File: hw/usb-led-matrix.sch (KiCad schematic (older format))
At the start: 103 parts, among them J1 USB_C_Receptacle_USB2.0, J2 Conn_ST_STDC14, U1 AP2210K-3.3, U2 STM32G473CET6, U3 74LVT245, U4 USBLC6-2P6, Y1 Crystal_GND24

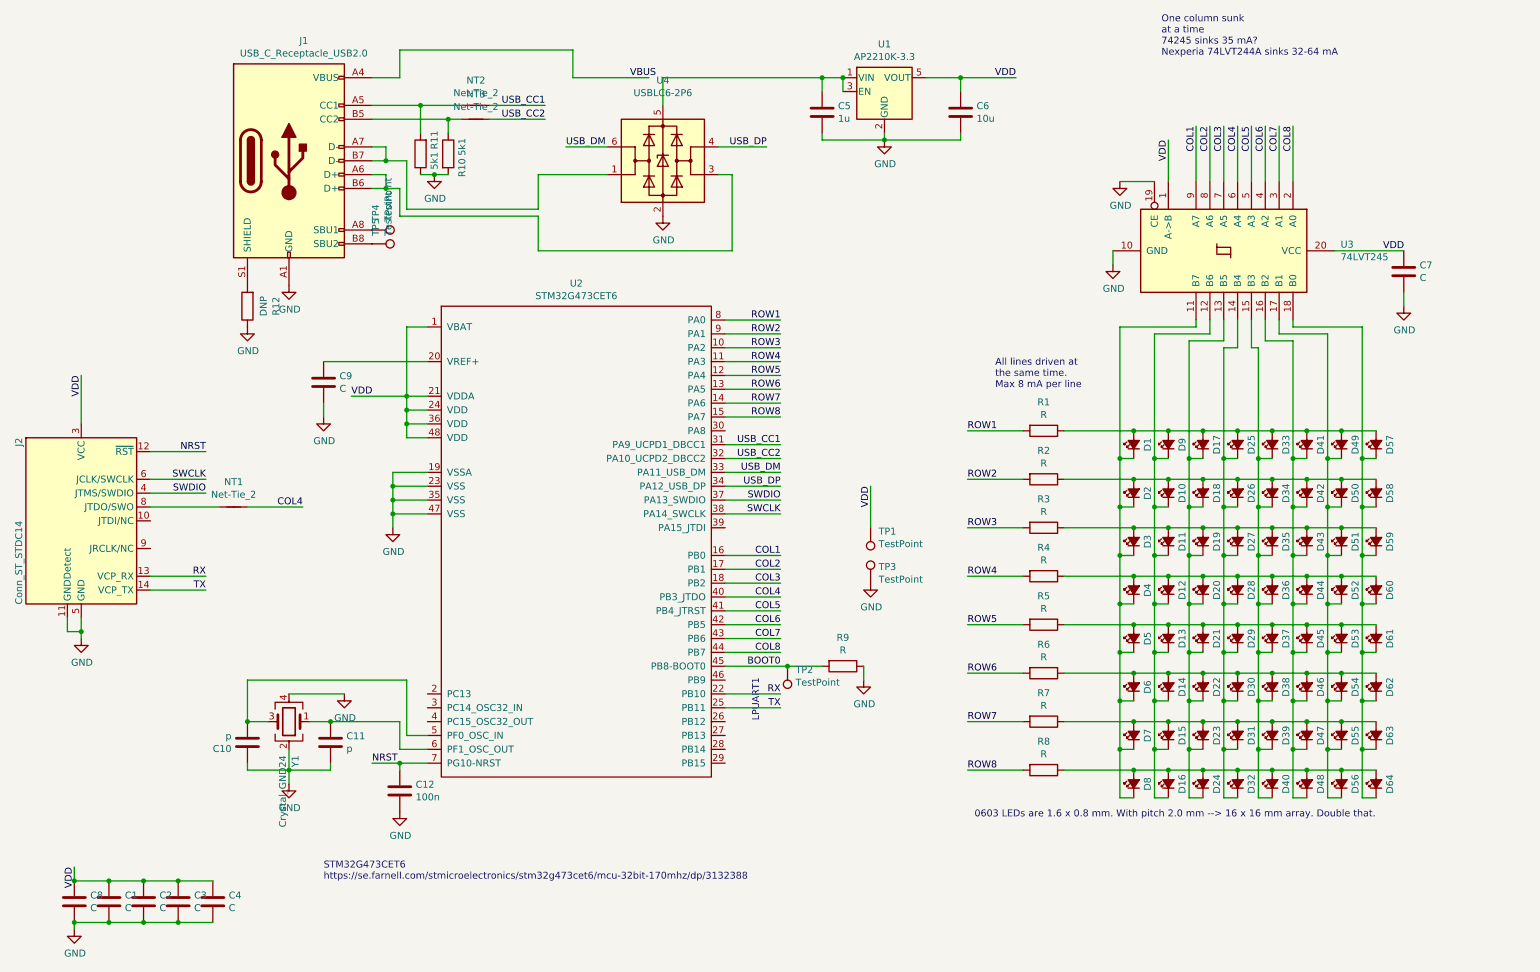
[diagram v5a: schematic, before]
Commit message: Four-layer board, update routing and some components
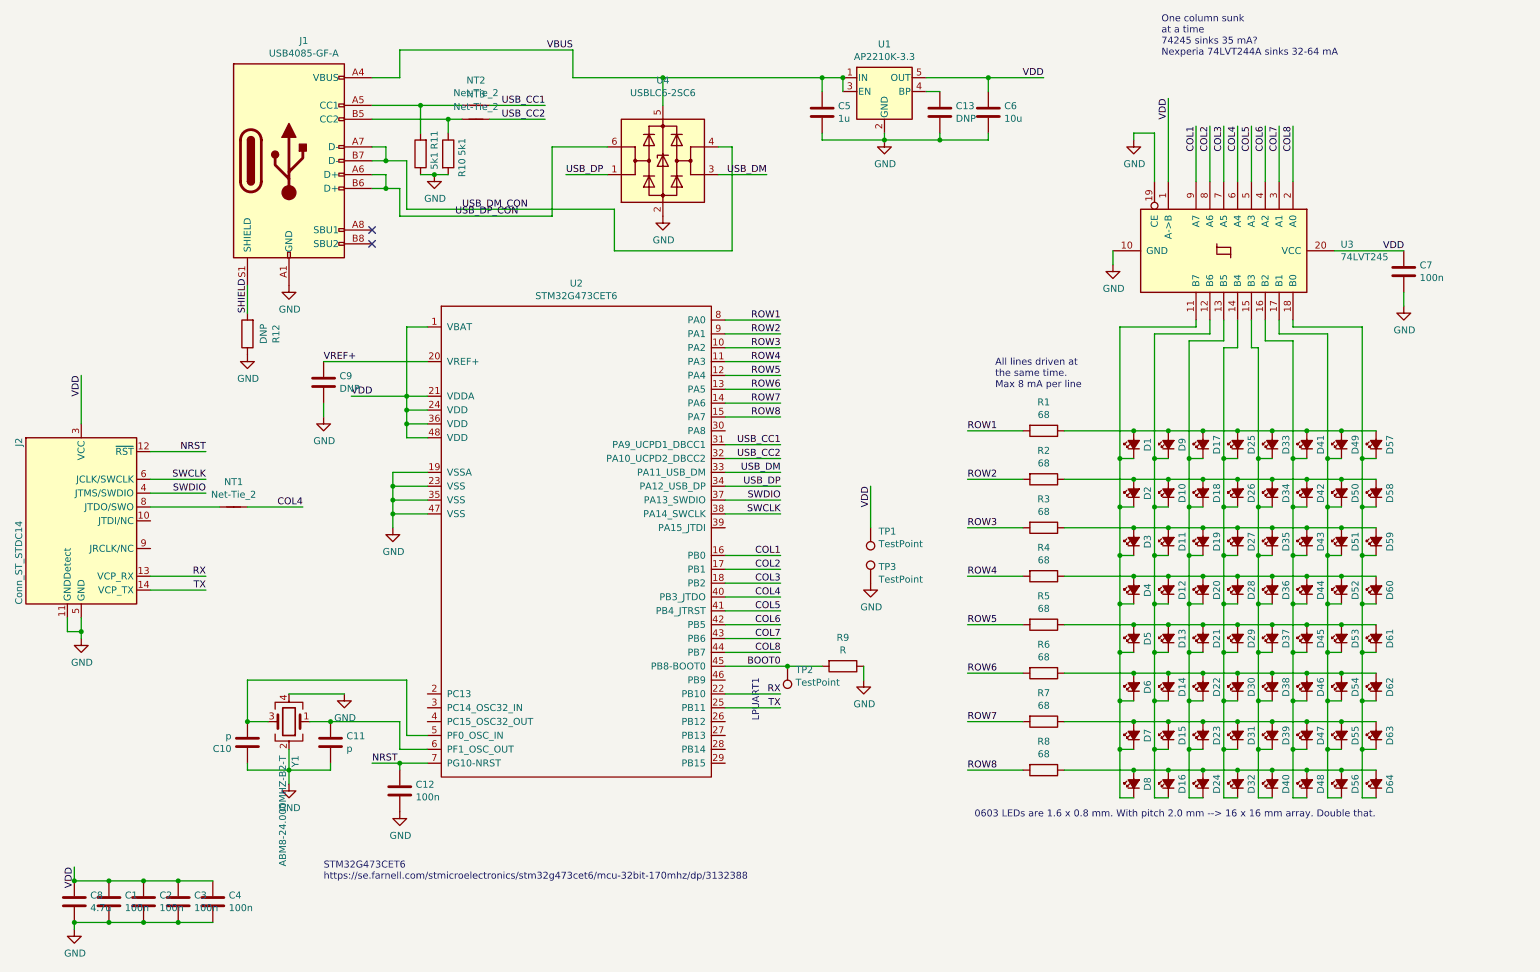
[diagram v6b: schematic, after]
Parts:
- removed TP4, TP5: TestPoint, TestPoint:TestPoint_Pad_1.0x1.0mm, symbol Connector:TestPoint
- removed U1: AP2210K-3.3, Package_TO_SOT_SMD:SOT-23-5, symbol Regulator_Linear:AP2204K-3.3
- removed U4: USBLC6-2P6, Package_TO_SOT_SMD:SOT-666, symbol Power_Protection:USBLC6-2P6
- added C13: DNP, Capacitor_SMD:C_0402_1005Metric_Pad0.74x0.62mm_HandSolder, symbol Device:C
- added U1: AP2210K-3.3, Package_TO_SOT_SMD:SOT-23-5, symbol Regulator_Linear:AP131-33
- added U4: USBLC6-2SC6, Package_TO_SOT_SMD:SOT-23-6, symbol Power_Protection:USBLC6-2SC6
- C1, C2, C3, C4, C7: value C -> 100n
- C8: value C -> 4.7u
- C9: value C -> DNP
- J1: value USB_C_Receptacle_USB2.0 -> USB4085-GF-A
- NT1, NT2, NT3: footprint NetTie:NetTie-2_SMD_Pad0.5mm -> Resistor_SMD:R_0201_0603Metric
- R1, R2, R3, R4, R5, R6, R7, R8: value R -> 68
- Y1: value Crystal_GND24 -> ABM8-24.000MHZ-B2-T
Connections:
- net GND: now also C13.2, U1.2 (GND), U4.2 (GND)
- net USB_DM: now also U4.3 (I/O2)
- net USB_DP: now also U4.1 (I/O1)
- net VBUS: now also C5.1, J1.A4 (VBUS), J1.A9 (VBUS), J1.B4 (VBUS), J1.B9 (VBUS), U1.1 (IN), U1.3 (EN), U4.5 (VBUS)
- net VDD: now also U1.5 (OUT)
- net USB_DP_CON: now reaches J1.A6 (D+), J1.B6 (D+)
- net USB_DP_CON: now also U4.6 (I/O1)
- net USB_DM_CON: now reaches J1.A7 (D-), J1.B7 (D-)
- net USB_DM_CON: now also U4.4 (I/O2)
- net SHIELD: now reaches J1.S1 (SHIELD), R12.2
- net VREF+: now reaches C9.1, U2.20 (VREF+)
- new net: C13.1, U1.4 (BP)
- no-connect marks 0 -> 2
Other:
- moved on the sheet: C6, R12

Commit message: Rearrange pins
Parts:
- removed NT1: Net-Tie_2, Resistor_SMD:R_0201_0603Metric, symbol Device:Net-Tie_2
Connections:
- net BOOT0 is gone; now on net ROW1: R9.2, TP2.1, U2.45 (PB8-BOOT0)
- net ROW1: no longer U2.8 (PA0)
- net ROW2: now also U2.46 (PB9); no longer U2.9 (PA1)
- net ROW3: now also U2.22 (PB10); no longer U2.10 (PA2)
- net ROW4: now also U2.25 (PB11); no longer U2.11 (PA3)
- net ROW5: now also U2.26 (PB12); no longer U2.12 (PA4)
- net ROW6: now also U2.27 (PB13); no longer U2.13 (PA5)
- net ROW7: now also U2.28 (PB14); no longer U2.14 (PA6)
- net ROW8: now also U2.29 (PB15); no longer U2.15 (PA7)
- net RX: now also U2.11 (PA3); no longer U2.22 (PB10)
- net TX: now also U2.10 (PA2); no longer U2.25 (PB11)
- no-connect marks 2 -> 5
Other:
- moved on the sheet: R9, TP2
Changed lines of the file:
@@
 USB_DP
 Wire Wire Line
-	5900 2850 6300 2850
-Wire Wire Line
-	5900 2950 6300 2950
-Wire Wire Line
-	5900 3050 6300 3050
-Wire Wire Line
-	5900 3150 6300 3150
-Wire Wire Line
-	5900 3250 6300 3250
-Wire Wire Line
-	5900 3350 6300 3350
-Wire Wire Line
-	5900 3450 6300 3450
-Wire Wire Line
-	5900 3550 6300 3550
-Text Label 6300 2850 2    50   ~ 0
+	5900 5450 6300 5450
+Wire Wire Line
+	5900 5550 6300 5550
+Wire Wire Line
+	5900 5650 6300 5650
+Wire Wire Line
+	5900 5750 6300 5750
+Wire Wire Line
+	5900 5850 6300 5850
+Wire Wire Line
+	5900 5950 6300 5950
+Wire Wire Line
+	5900 6050 6300 6050
+Text Label 6300 5350 2    50   ~ 0
 ROW1
-Text Label 6300 2950 2    50   ~ 0
+Text Label 6300 5450 2    50   ~ 0
 ROW2
-Text Label 6300 3050 2    50   ~ 0
+Text Label 6300 5550 2    50   ~ 0
 ROW3
-Text Label 6300 3150 2    50   ~ 0
+Text Label 6300 5650 2    50   ~ 0
 ROW4
-Text Label 6300 3250 2    50   ~ 0
+Text Label 6300 5750 2    50   ~ 0
 ROW5
-Text Label 6300 3350 2    50   ~ 0
+Text Label 6300 5850 2    50   ~ 0
 ROW6
-Text Label 6300 3450 2    50   ~ 0
+Text Label 6300 5950 2    50   ~ 0
 ROW7
-Text Label 6300 3550 2    50   ~ 0
+Text Label 6300 6050 2    50   ~ 0
 ROW8
 Wire Wire Line
@@
 L Device:R R9
 U 1 1 6036EDA7
-P 6750 5350
-F 0 "R9" V 6543 5350 50  0000 C CNN
-F 1 "R" V 6634 5350 50  0000 C CNN
-F 2 "Resistor_SMD:R_0402_1005Metric_Pad0.72x0.64mm_HandSolder" V 6680 5350 50  0001 C CNN
-F 3 "~" H 6750 5350 50  0001 C CNN
-	1    6750 5350
+P 7100 5350
+F 0 "R9" V 6893 5350 50  0000 C CNN
+F 1 "R" V 6984 5350 50  0000 C CNN
+F 2 "Resistor_SMD:R_0402_1005Metric_Pad0.72x0.64mm_HandSolder" V 7030 5350 50  0001 C CNN
+F 3 "~" H 7100 5350 50  0001 C CNN
+	1    7100 5350
 	0    1    1    0
 $EndComp
 Wire Wire Line
-	5900 5350 6350 5350
-Text Label 6300 5350 2    50   ~ 0
-BOOT0
-Wire Wire Line
-	5900 5650 6300 5650
-Wire Wire Line
-	5900 5550 6300 5550
-Text Label 6300 5650 2    50   ~ 0
+	5900 3050 6300 3050
+Wire Wire Line
+	5900 3150 6300 3150
+Text Label 6300 3050 2    50   ~ 0
 TX
 $Comp
@@
 Text Label 4800 900  2    50   ~ 0
 VBUS
-Text Label 6300 5550 2    50   ~ 0
+Text Label 6300 3150 2    50   ~ 0
 RX
 $Comp
@@
 L power:GND #PWR0109
 U 1 1 6068EE74
-P 6900 5450
-F 0 "#PWR0109" H 6900 5200 50  0001 C CNN
-F 1 "GND" H 6905 5277 50  0000 C CNN
-F 2 "" H 6900 5450 50  0001 C CNN
-F 3 "" H 6900 5450 50  0001 C CNN
-	1    6900 5450
-	1    0    0    -1
-$EndComp
-Wire Wire Line
-	6900 5350 6900 5450
+P 7250 5450
+F 0 "#PWR0109" H 7250 5200 50  0001 C CNN
+F 1 "GND" H 7255 5277 50  0000 C CNN
+F 2 "" H 7250 5450 50  0001 C CNN
+F 3 "" H 7250 5450 50  0001 C CNN
+	1    7250 5450
+	1    0    0    -1
+$EndComp
+Wire Wire Line
+	7250 5350 7250 5450
 $Comp
 L Device:C C9
@@
 L Connector:TestPoint TP2
 U 1 1 6086B887
-P 6350 5350
-F 0 "TP2" H 6292 5376 50  0000 R CNN
-F 1 "TestPoint" H 6292 5467 50  0000 R CNN
-F 2 "TestPoint:TestPoint_THTPad_D1.0mm_Drill0.5mm" H 6550 5350 50  0001 C CNN
-F 3 "~" H 6550 5350 50  0001 C CNN
-	1    6350 5350
+P 6700 5350
+F 0 "TP2" H 6642 5376 50  0000 R CNN
+F 1 "TestPoint" H 6642 5467 50  0000 R CNN
+F 2 "TestPoint:TestPoint_THTPad_D1.0mm_Drill0.5mm" H 6900 5350 50  0001 C CNN
+F 3 "~" H 6900 5350 50  0001 C CNN
+	1    6700 5350
 	-1   0    0    1
 $EndComp
@@
 Text Label 9100 1250 3    50   ~ 0
 VDD
-Connection ~ 6350 5350
 $Comp
 L Connector:TestPoint TP3
@@
 Wire Wire Line
 	2750 6100 2750 5950
-Wire Wire Line
-	2450 4200 2850 4200
-Text Label 2850 4200 2    50   ~ 0
-COL4
-$Comp
-L Device:Net-Tie_2 NT1
-U 1 1 6014E81B
-P 2350 4200
-F 0 "NT1" H 2350 4381 50  0000 C CNN
-F 1 "Net-Tie_2" H 2350 4290 50  0000 C CNN
-F 2 "Resistor_SMD:R_0201_0603Metric" H 2350 4200 50  0001 C CNN
-F 3 "~" H 2350 4200 50  0001 C CNN
-	1    2350 4200
-	1    0    0    -1
-$EndComp
-Wire Wire Line
-	1750 4200 2250 4200
 $Comp
 L Device:R R12
@@
 $EndComp
 Wire Wire Line
-	6350 5350 6600 5350
-Text Notes 6150 5750 1    50   ~ 0
+	6700 5350 6950 5350
+Text Notes 6400 3250 1    50   ~ 0
 LPUART1
 Wire Wire Line
@@
 Wire Wire Line
 	9100 1250 9100 1850
+Wire Wire Line
+	5900 5350 6700 5350
+Connection ~ 6700 5350
+NoConn ~ 1750 4200
+NoConn ~ 1750 4300
+NoConn ~ 1750 4500
 $EndSCHEMATC

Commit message: Update routing
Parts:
- added R13: R, Resistor_SMD:R_0402_1005Metric_Pad0.72x0.64mm_HandSolder, symbol Device:R
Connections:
- net GND: no longer U3.19 (CE)
- net VDD: now also R13.2
- net BUFFER_EN: now reaches U2.8 (PA0)
- net BUFFER_EN: now also U3.19 (CE), R13.1
- net USB_DM renamed USB_D-
- net USB_DM_CON renamed USBCON_D-
- net USB_DP renamed USB_D+
- net USB_DP_CON renamed USBCON_D+
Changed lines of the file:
@@
 Text Notes 7850 3350 0    50   ~ 0
 All lines driven at\nthe same time.\nMax 8 mA per line
-Text Notes 9050 950  0    50   ~ 0
+Text Notes 9700 1300 0    50   ~ 0
 One column sunk\nat a time\n74245 sinks 35 mA?\nNexperia 74LVT244A sinks 32-64 mA
 Text Notes 3000 6900 0    50   ~ 0
@@
 	5900 4050 6300 4050
 Text Label 6300 3950 2    50   ~ 0
-USB_DM
+USB_D-
 Text Label 6300 4050 2    50   ~ 0
-USB_DP
+USB_D+
 Wire Wire Line
 	5900 5450 6300 5450
@@
 	3600 5850 3750 5850
 Text Label 6200 1800 2    50   ~ 0
-USB_DM
+USB_D-
 Text Label 4750 1800 0    50   ~ 0
-USB_DP
+USB_D+
 Wire Wire Line
 	3350 1800 3450 1800
@@
 Text Label 6950 4050 3    50   ~ 0
 VDD
-$Comp
-L power:GND #PWR0111
-U 1 1 608B0F92
-P 8850 1550
-F 0 "#PWR0111" H 8850 1300 50  0001 C CNN
-F 1 "GND" H 8855 1377 50  0000 C CNN
-F 2 "" H 8850 1550 50  0001 C CNN
-F 3 "" H 8850 1550 50  0001 C CNN
-	1    8850 1550
-	1    0    0    -1
-$EndComp
-Text Label 9100 1250 3    50   ~ 0
+Text Label 9100 800  0    50   ~ 0
 VDD
 $Comp
@@
 Connection ~ 3450 1900
 Wire Wire Line
-	8850 1550 8850 1500
-Wire Wire Line
-	8850 1500 9000 1500
-Wire Wire Line
 	4800 1100 5450 1100
 Connection ~ 5450 1100
@@
 	5950 1600 5850 1600
 Text Label 4000 2050 0    50   ~ 0
-USB_DM_CON
+USBCON_D-
 Text Label 3950 2100 0    50   ~ 0
-USB_DP_CON
+USBCON_D+
 $Comp
 L Power_Protection:USBLC6-2SC6 U4
@@
 SHIELD
 Wire Wire Line
-	9000 1500 9000 1850
-Wire Wire Line
-	9100 1250 9100 1850
-Wire Wire Line
 	5900 5350 6700 5350
 Connection ~ 6700 5350
@@
 NoConn ~ 1750 4300
 NoConn ~ 1750 4500
+Text Label 9000 1250 3    50   ~ 0
+BUFFER_EN
+Text Label 6300 2850 2    50   ~ 0
+BUFFER_EN
+Wire Wire Line
+	5900 2850 6300 2850
+$Comp
+L Device:R R13
+U 1 1 61564A09
+P 9000 1100
+F 0 "R13" V 8793 1100 50  0000 C CNN
+F 1 "R" V 8884 1100 50  0000 C CNN
+F 2 "Resistor_SMD:R_0402_1005Metric_Pad0.72x0.64mm_HandSolder" V 8930 1100 50  0001 C CNN
+F 3 "~" H 9000 1100 50  0001 C CNN
+	1    9000 1100
+	-1   0    0    1
+$EndComp
+Wire Wire Line
+	9000 1250 9000 1850
+Wire Wire Line
+	9100 800  9100 950
+Wire Wire Line
+	9000 950  9100 950
+Connection ~ 9100 950
+Wire Wire Line
+	9100 950  9100 1850
 $EndSCHEMATC
